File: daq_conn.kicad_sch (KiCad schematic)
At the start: 161 parts

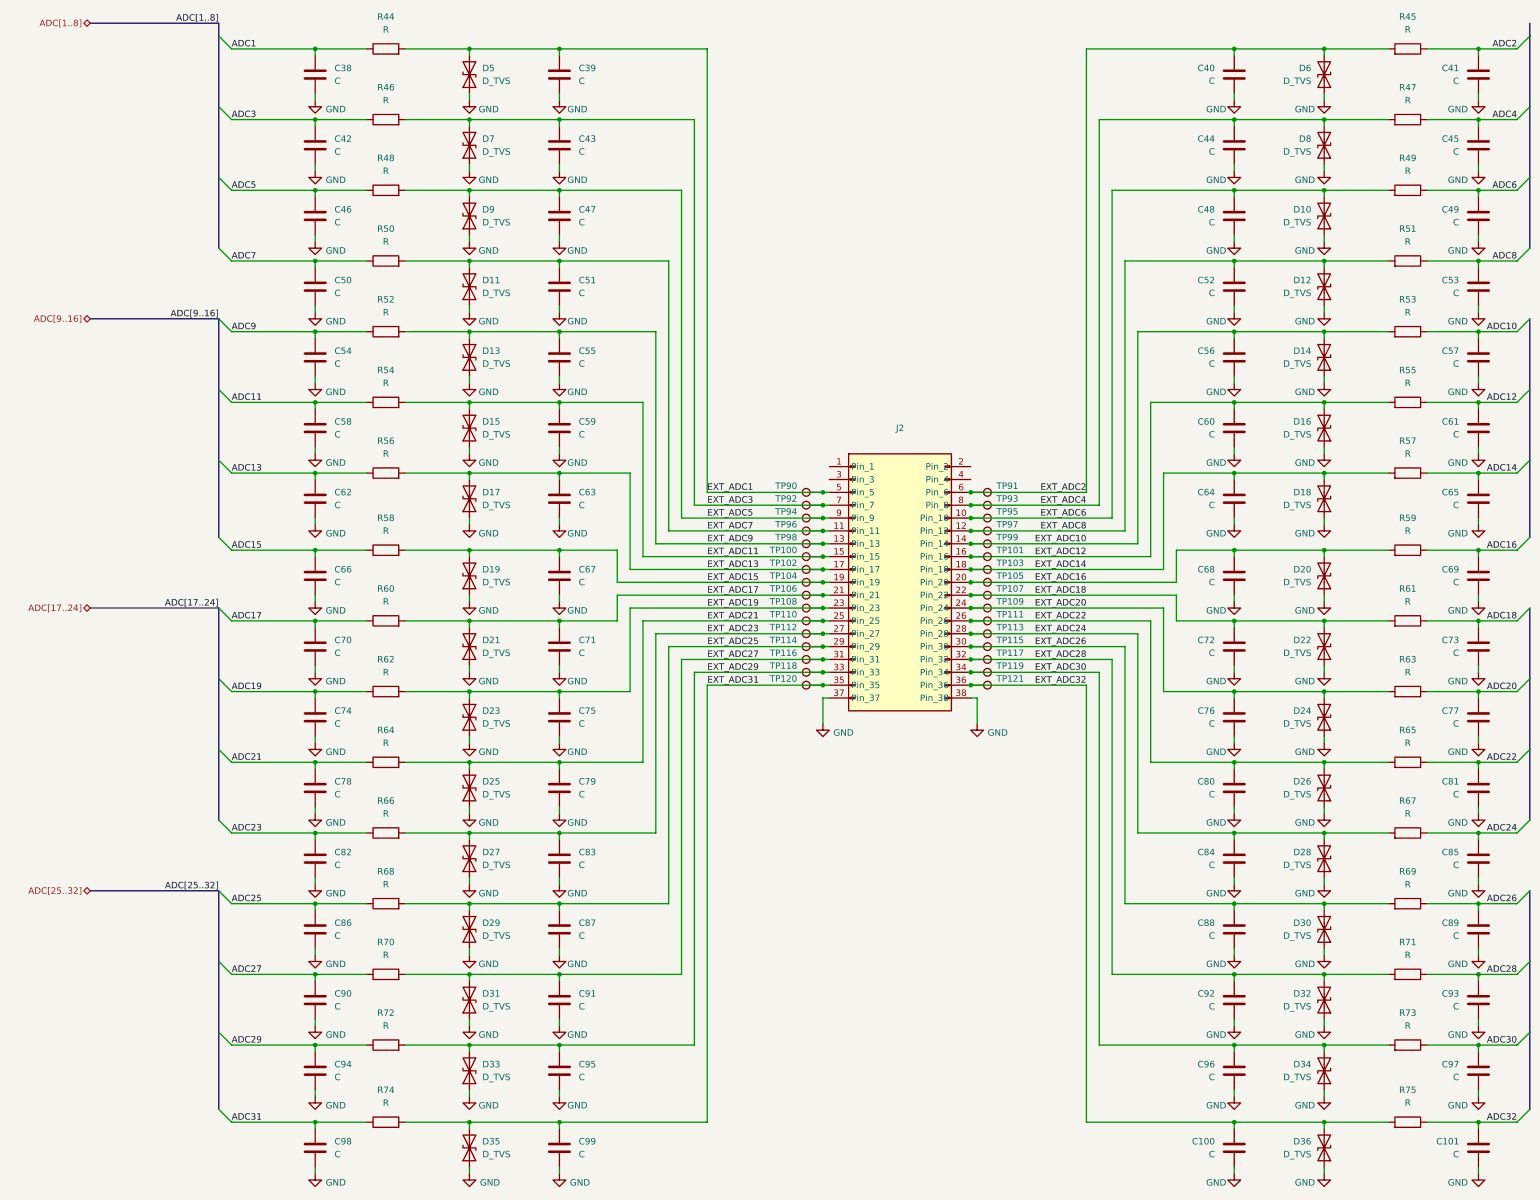
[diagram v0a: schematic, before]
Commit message: did stuff, amongst others changed to op-amp input filter
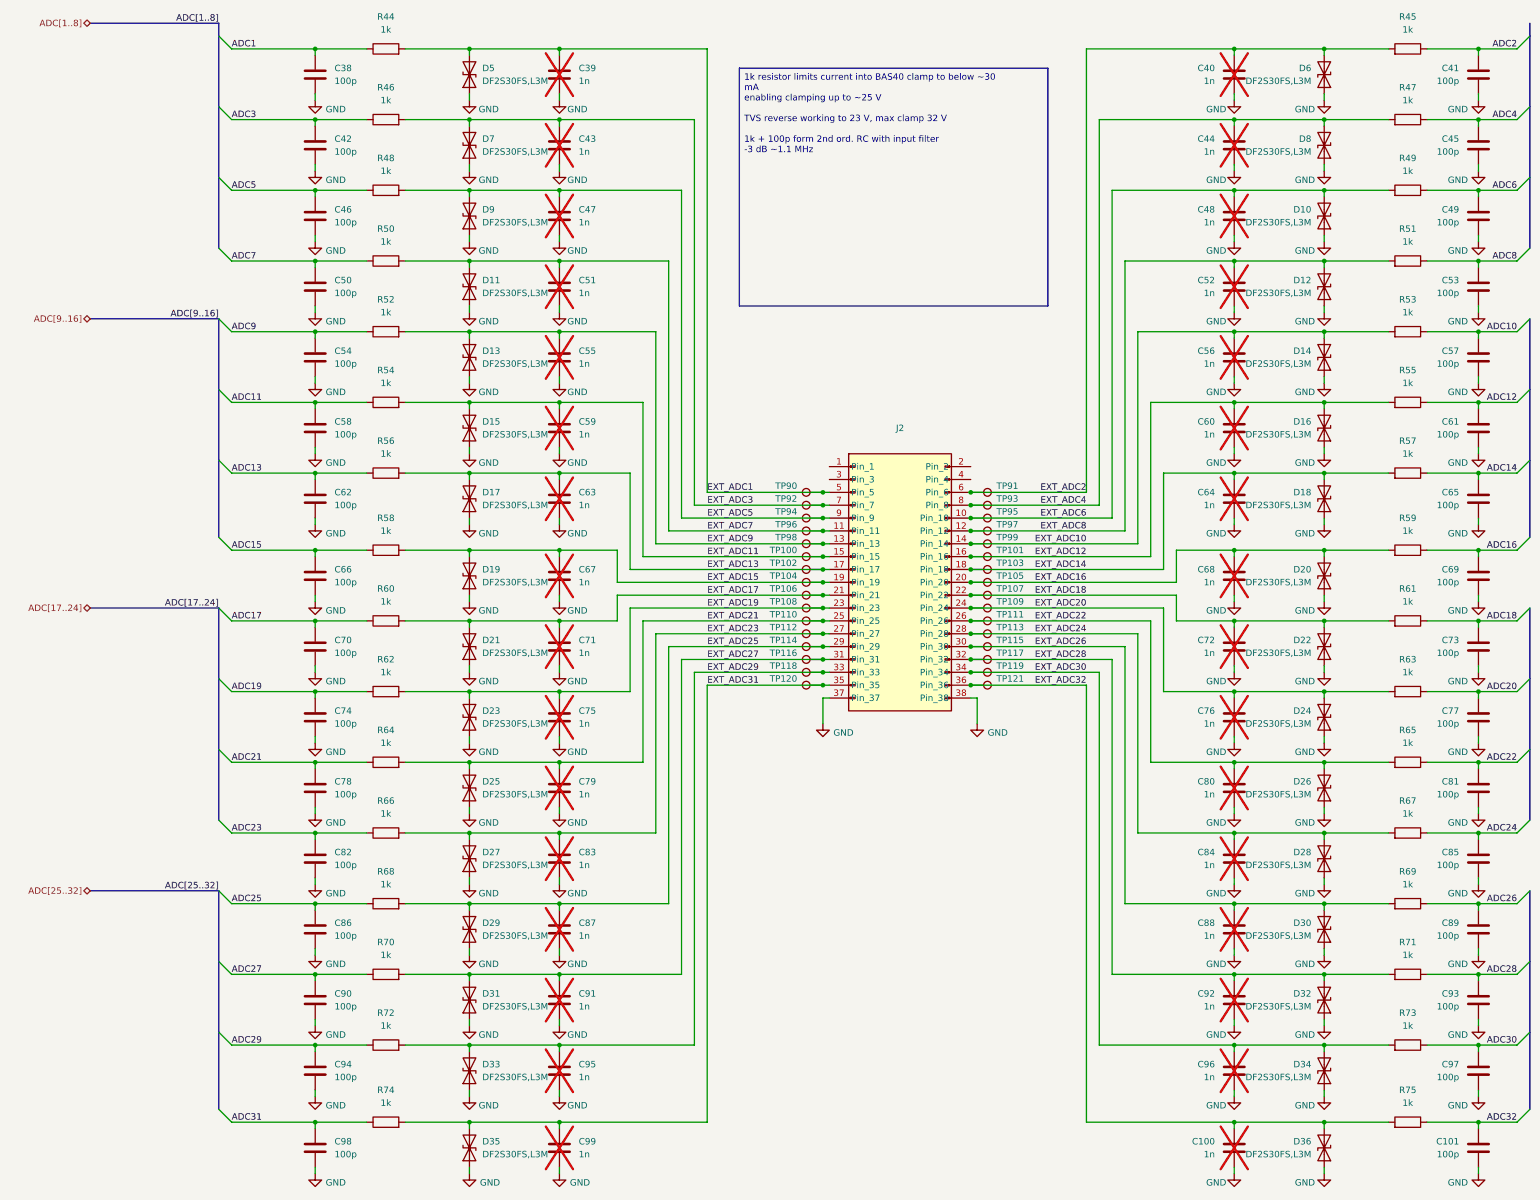
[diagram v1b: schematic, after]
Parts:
- C100, C39, C40, C43, C44, C47, C48, C51, C52, C55, C56, C59, C60, C63, C64, C67, C68, C71, C72, C75, C76, C79, C80, C83, C84, C87, C88, C91, C92, C95, C96, C99: value C -> 1n; now not fitted
- C101, C38, C41, C42, C45, C46, C49, C50, C53, C54, C57, C58, C61, C62, C65, C66, C69, C70, C73, C74, C77, C78, C81, C82, C85, C86, C89, C90, C93, C94, C97, C98: value C -> 100p; LCSC (none) -> C1546; LCSC Basic/Pref (none) -> x; LCSC Part (none) -> C1546
- D10, D11, D12, D13, D14, D15, D16, D17, D18, D19, D20, D21, D22, D23, D24, D25, D26, D27, D28, D29, D30, D31, D32, D33, D34, D35, D36, D5, D6, D7, D8, D9: value D_TVS -> DF2S30FS,L3M; LCSC (none) -> C1973663; LCSC Part (none) -> C1973663
- R44, R45, R46, R47, R48, R49, R50, R51, R52, R53, R54, R55, R56, R57, R58, R59, R60, R61, R62, R63, R64, R65, R66, R67, R68, R69, R70, R71, R72, R73, R74, R75: value R -> 1k; footprint Resistor_SMD:R_0603_1608Metric -> Resistor_SMD:R_1210_3225Metric; LCSC (none) -> C5576460; LCSC Basic/Pref (none) -> n; LCSC Part (none) -> C5576460
